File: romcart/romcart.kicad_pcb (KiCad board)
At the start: 2 copper layers, 72 x 50.2 mm, 7 parts, among them J1 Proto Connector, SW1 SW_SPDT, U1 27C512, U2 SG-1000-Cart

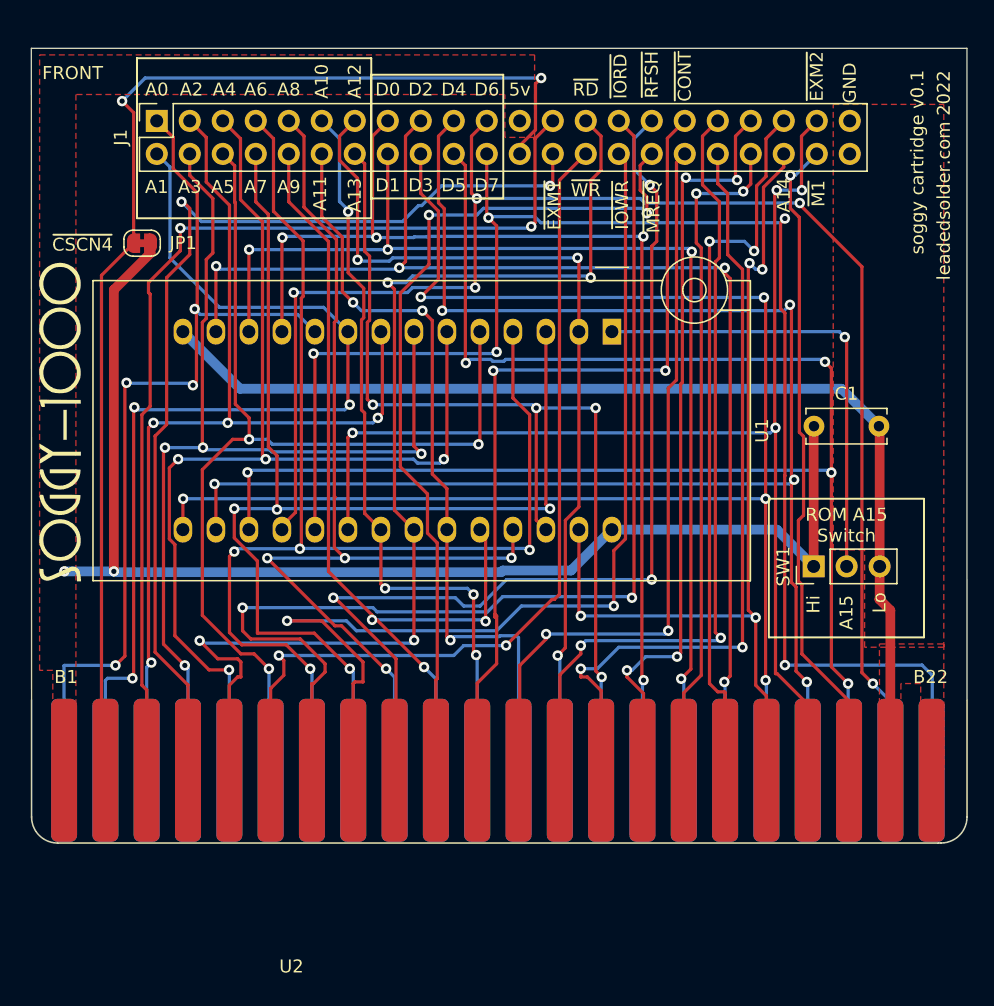
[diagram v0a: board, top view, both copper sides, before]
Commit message: Provide 1.6mm clearance for fingers so bevel is easier
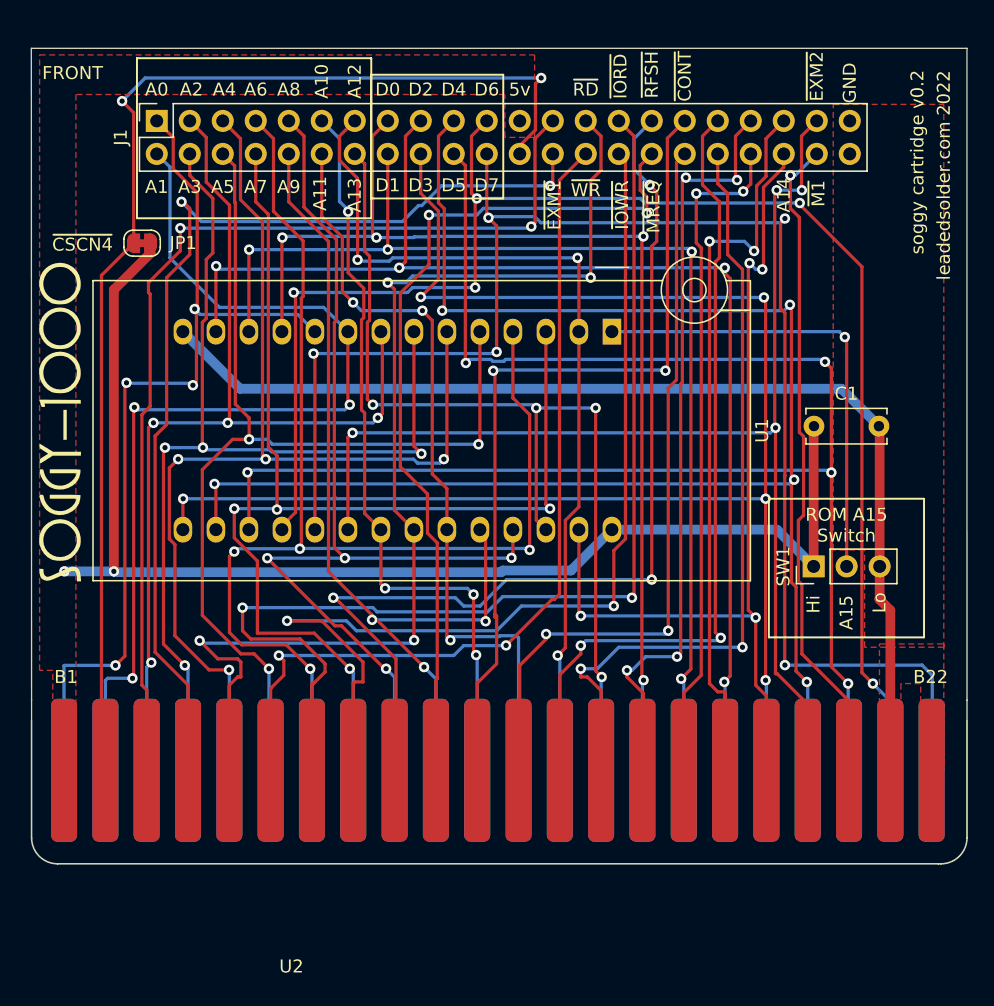
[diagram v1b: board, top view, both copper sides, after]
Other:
- board size 72 x 50.2 mm -> 72 x 51.8 mm
- board text added: "soggy cartridge v0.2"
- board text removed: "soggy cartridge v0.1"

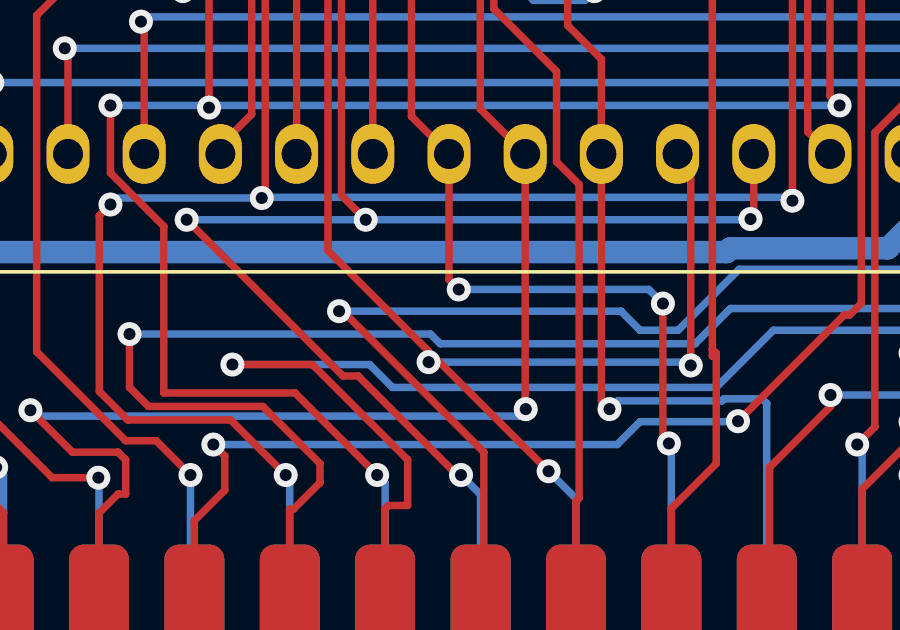
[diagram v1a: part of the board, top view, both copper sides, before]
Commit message: Try to make board as wide as keyboard conn, 6mm keepout
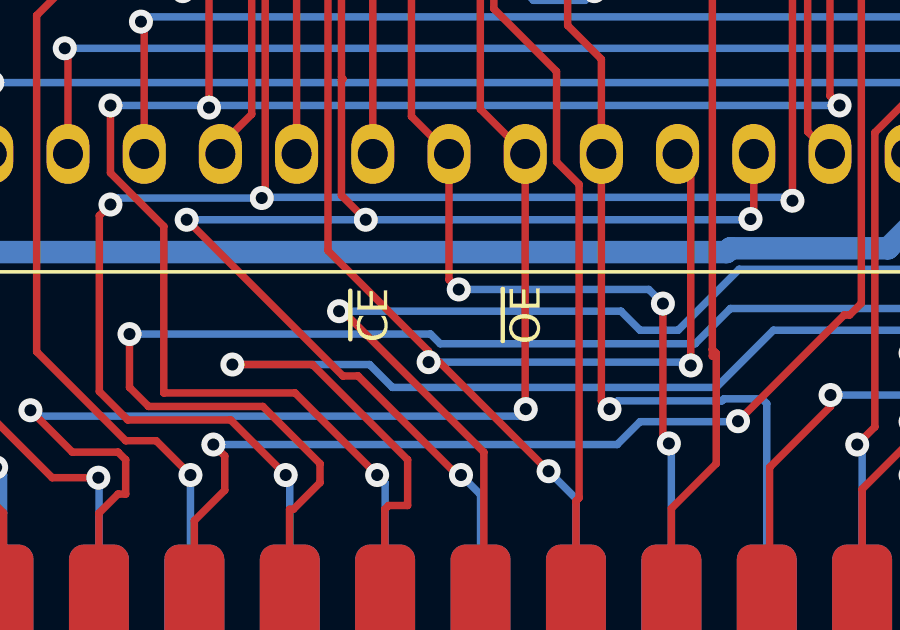
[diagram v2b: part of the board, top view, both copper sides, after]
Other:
- board text added: "~{CE}"
- board text added: "~{OE}"
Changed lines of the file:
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@@
+    (effects (font (size 1 1) (thickness 0.15)))
+  )
+  (gr_text "~{OE}" (at 146.685 114.935 90) (layer "F.SilkS")
     (effects (font (size 1 1) (thickness 0.15)))
   )
@@
     (effects (font (size 1 1) (thickness 0.15)))
   )
+  (gr_text "~{CE}" (at 141.605 114.935 90) (layer "F.SilkS")
+    (effects (font (size 1 1) (thickness 0.15)))
+  )

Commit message: Sub-project links
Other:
- board text added: "(27c512 only)"
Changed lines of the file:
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@@
+    (effects (font (size 1 1) (thickness 0.15)))
+  )
+  (gr_text "(27c512 only)" (at 180.086 118.745) (layer "F.SilkS")
     (effects (font (size 1 1) (thickness 0.15)))
   )
